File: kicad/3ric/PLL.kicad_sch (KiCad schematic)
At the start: 12 parts

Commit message: update schematics
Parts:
- removed U? (x3): 74LS11, symbol 74xx:74LS11
- removed U_NOT_DECODE? (x2): 74LS14, Package_DIP:DIP-14_W7.62mm_Socket, symbol 74xx:74LS14
- added U? (x3): 74LS20, symbol 74xx:74LS20
- R?: value R430 -> 51
- R?: value R10K -> 30
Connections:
- net GND: now also U?.5 (Inh), U?.10, U?.12, U?.13, U?.7 (GND), U?.9
- net PHI7: now also U?.2 (CP), U?.4 (FOUT)
- net VCC: now also U?.14 (VCC); no longer U?.5 (Inh)
- net at U?.1 (~{MR}): now also U?.6
- net at U?.12 (Q2): now also U?.4, U?.5; no longer U?.3 (RefIn)
- net at U?.13 (Q1): now also U?.2
- net at U?.14 (Q0): now also U?.1
- net at R?.1, U?.13 (PC2): now also U?.9 (VCOin)
- net at C?.1, R?.2: no longer U?.9 (VCOin)
- no-connect marks 0 -> 11
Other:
- moved on the sheet: C?, R?

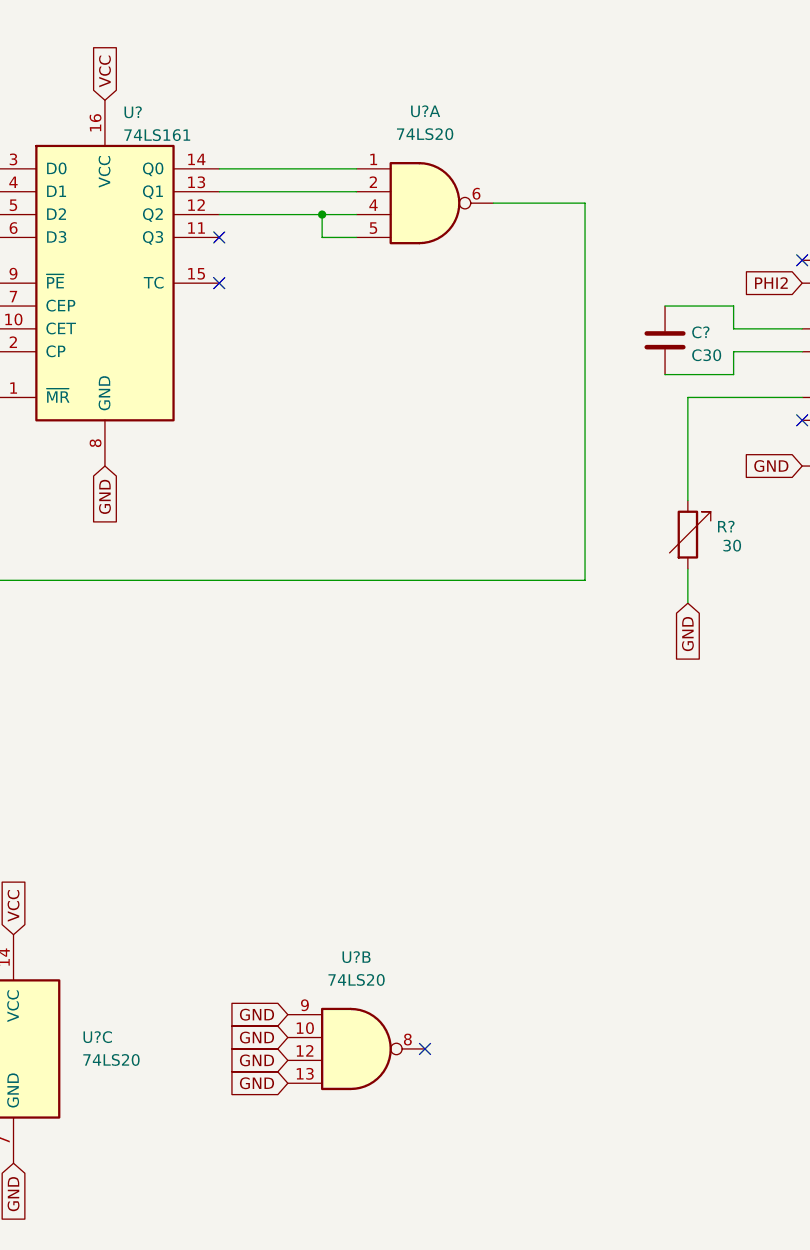
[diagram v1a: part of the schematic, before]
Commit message: upgraded to kicad 8, updates to schematic - added snes controllers, mouse port, many fixes
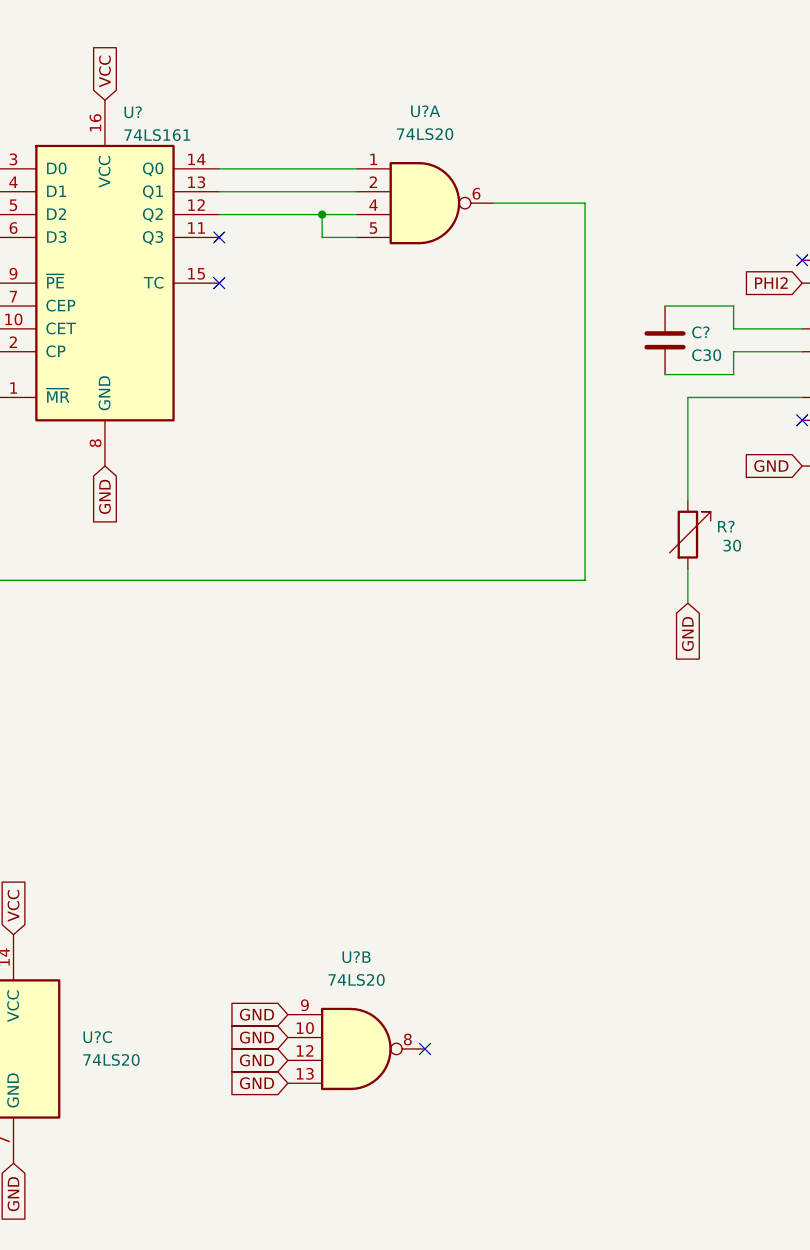
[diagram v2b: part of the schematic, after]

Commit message: wiring continued
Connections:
- net at U?.13 (Q1), U?.2: now also U?.3 (RefIn)
- no-connect marks 11 -> 10
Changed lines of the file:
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@@
 	(paper "A4")
+	(junction
+		(at 101.6 74.93)
+		(diameter 0)
+		(color 0 0 0 0)
+	)
 	(junction
 		(at 198.12 82.55)
@@
 	)
 	(no_connect
-		(at 154.94 82.55)
-	)
-	(no_connect
 		(at 64.77 72.39)
 	)
@@
 	(wire
 		(pts
+			(xy 101.6 62.23) (xy 101.6 74.93)
+		)
+		(stroke
+			(width 0)
+			(type default)
+		)
+	)
+	(wire
+		(pts
 			(xy 180.34 100.33) (xy 184.15 100.33)
 		)
@@
 	(wire
 		(pts
+			(xy 101.6 74.93) (xy 105.41 74.93)
+		)
+		(stroke
+			(width 0)
+			(type default)
+		)
+	)
+	(wire
+		(pts
 			(xy 147.32 92.71) (xy 147.32 95.25)
 		)
@@
 	(wire
 		(pts
+			(xy 154.94 62.23) (xy 101.6 62.23)
+		)
+		(stroke
+			(width 0)
+			(type default)
+		)
+	)
+	(wire
+		(pts
 			(xy 199.39 106.68) (xy 199.39 110.49)
 		)
@@
 	(wire
 		(pts
-			(xy 90.17 74.93) (xy 105.41 74.93)
-		)
-		(stroke
+			(xy 90.17 74.93) (xy 101.6 74.93)
+		)
+		(stroke
+			(width 0)
+			(type default)
+		)
+	)
+	(wire
+		(pts
+			(xy 154.94 82.55) (xy 154.94 62.23)
+		)
+		(stroke

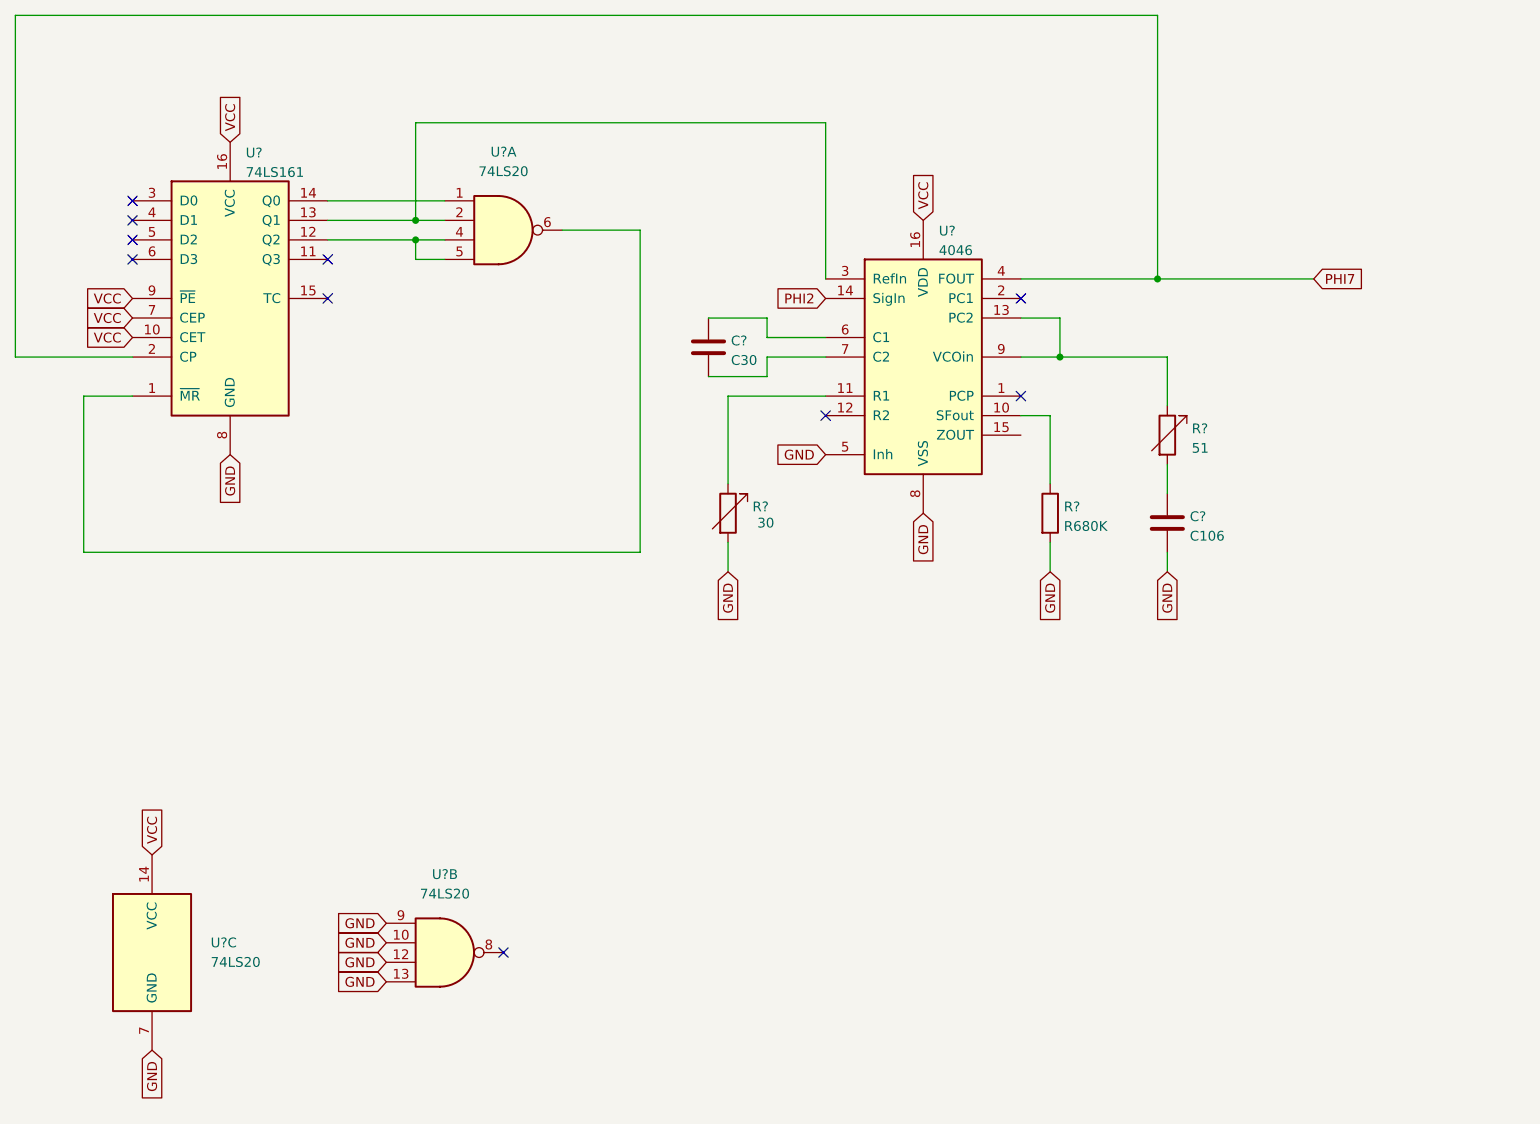
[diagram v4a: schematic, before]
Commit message: update schematic based on breadboard
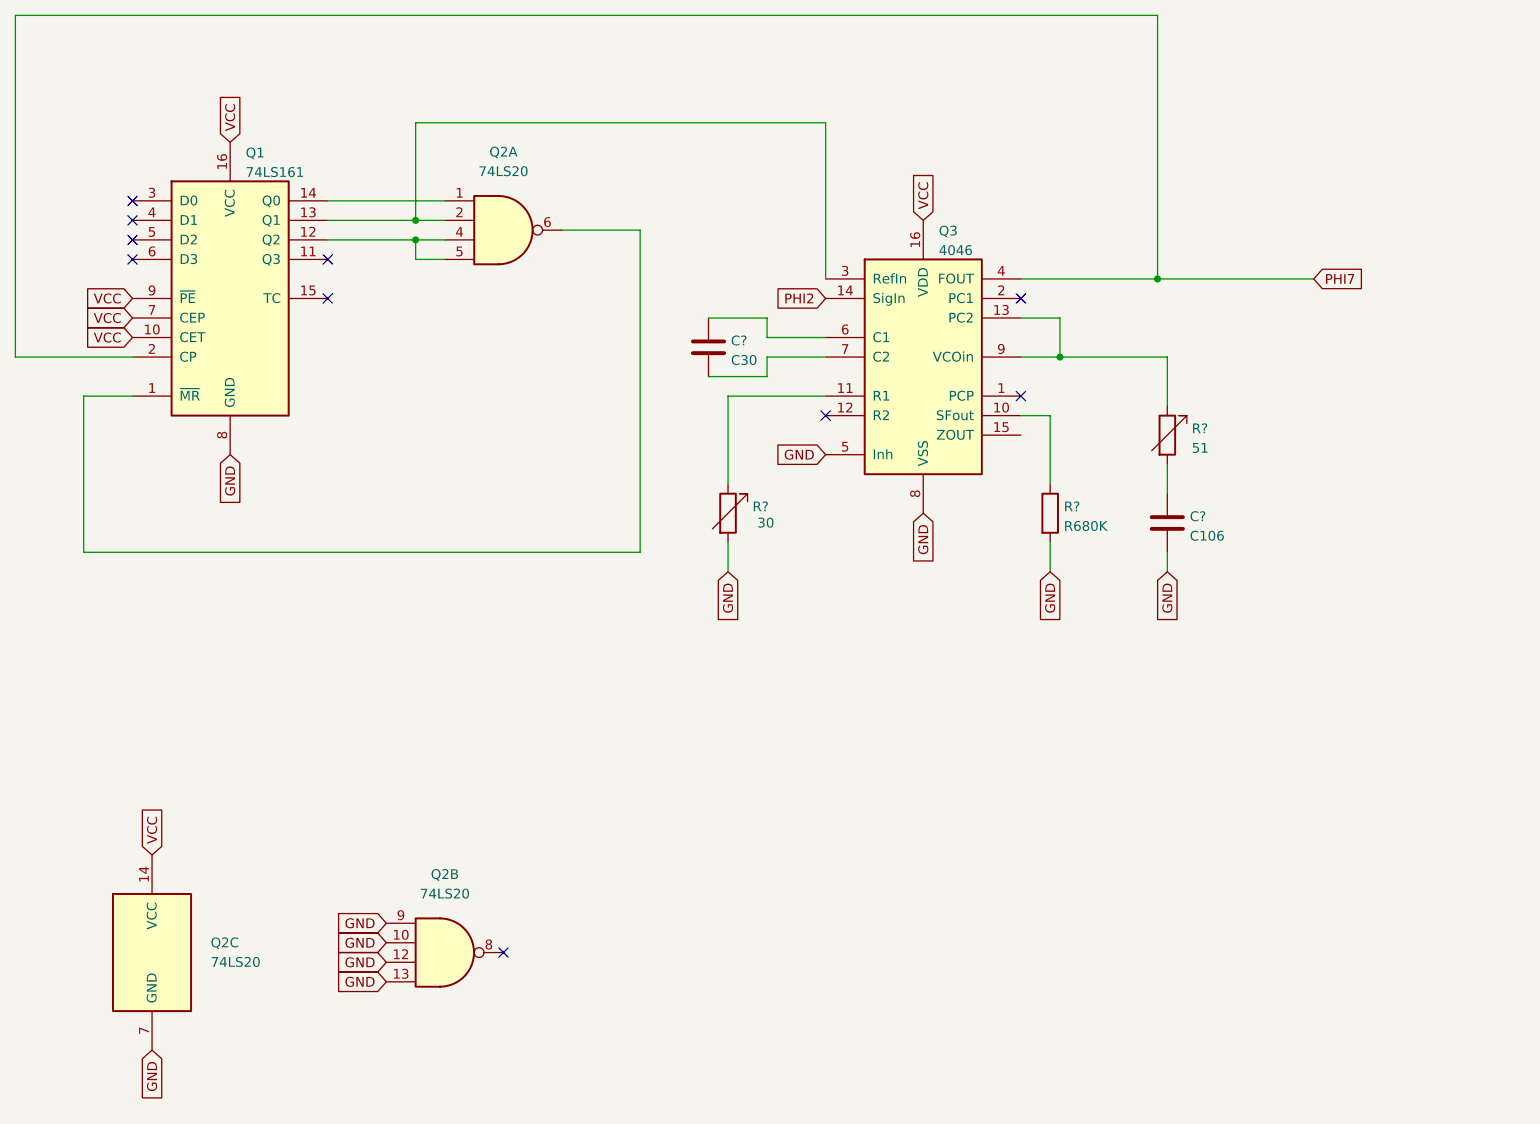
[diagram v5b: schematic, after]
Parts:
- gave numbers to parts that had none: 3
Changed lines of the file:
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@@
 		(dnp no)
 		(fields_autoplaced yes)
-		(property "Reference" "U?"
+		(property "Reference" "Q1"
 			(at 79.4894 66.1502 0)
 			(effects
@@
 			(project "3ric"
 				(path "/e63e39d7-6ac0-4ffd-8aa3-1841a4541b55/f1111e82-0abc-4d93-b82c-5bd5a885becb"
-					(reference "U?")
+					(reference "Q1")
 					(unit 1)
 				)
@@
 		(dnp no)
 		(fields_autoplaced yes)
-		(property "Reference" "U?"
+		(property "Reference" "Q2"
 			(at 113.03 66.04 0)
 			(effects
@@
 			(project "3ric"
 				(path "/e63e39d7-6ac0-4ffd-8aa3-1841a4541b55/f1111e82-0abc-4d93-b82c-5bd5a885becb"
-					(reference "U?")
+					(reference "Q2")
 					(unit 1)
 				)
@@
 		(dnp no)
 		(fields_autoplaced yes)
-		(property "Reference" "U?"
+		(property "Reference" "Q3"
 			(at 169.6594 76.3102 0)
 			(effects
@@
 			(project "3ric"
 				(path "/e63e39d7-6ac0-4ffd-8aa3-1841a4541b55/f1111e82-0abc-4d93-b82c-5bd5a885becb"
-					(reference "U?")
+					(reference "Q3")
 					(unit 1)
 				)
@@
 		(dnp no)
 		(fields_autoplaced yes)
-		(property "Reference" "U?"
+		(property "Reference" "Q2"
 			(at 105.41 160.02 0)
 			(effects
@@
 			(project "3ric"
 				(path "/e63e39d7-6ac0-4ffd-8aa3-1841a4541b55/f1111e82-0abc-4d93-b82c-5bd5a885becb"
-					(reference "U?")
+					(reference "Q2")
 					(unit 2)
 				)
@@
 		(dnp no)
 		(fields_autoplaced yes)
-		(property "Reference" "U?"
+		(property "Reference" "Q2"
 			(at 74.93 168.9099 0)
 			(effects
@@
 			(project "3ric"
 				(path "/e63e39d7-6ac0-4ffd-8aa3-1841a4541b55/f1111e82-0abc-4d93-b82c-5bd5a885becb"
-					(reference "U?")
+					(reference "Q2")
 					(unit 3)
 				)

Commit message: cleaning up of the schematic
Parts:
- C3, C4: renamed from C?; footprint (none) -> Capacitor_THT:C_Axial_L3.8mm_D2.6mm_P7.50mm_Horizontal
- Q1, Q3: footprint (none) -> Package_DIP:DIP-16_W7.62mm_Socket
- Q2: footprint (none) -> Package_DIP:DIP-14_W7.62mm_Socket
- R34, R35, R36: renamed from R?; footprint (none) -> Resistor_THT:R_Axial_DIN0207_L6.3mm_D2.5mm_P7.62mm_Horizontal
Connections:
- no-connect marks 10 -> 11
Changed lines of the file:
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@@
+	)
+	(no_connect
+		(at 180.34 102.87)
 	)
 	(no_connect
@@
 			)
 		)
-		(property "Footprint" ""
+		(property "Footprint" "Package_DIP:DIP-16_W7.62mm_Socket"
 			(at 77.47 85.09 0)
 			(effects
@@
 			)
 		)
-		(property "Footprint" ""
+		(property "Footprint" "Package_DIP:DIP-14_W7.62mm_Socket"
 			(at 113.03 76.2 0)
 			(effects
@@
 		(on_board yes)
 		(dnp no)
-		(property "Reference" "R?"
+		(property "Reference" "R35"
 			(at 185.928 112.1953 0)
 			(effects
@@
 			)
 		)
-		(property "Footprint" ""
+		(property "Footprint" "Resistor_THT:R_Axial_DIN0207_L6.3mm_D2.5mm_P7.62mm_Horizontal"
 			(at 182.372 113.03 90)
 			(effects
@@
 			(project "3ric"
 				(path "/e63e39d7-6ac0-4ffd-8aa3-1841a4541b55/f1111e82-0abc-4d93-b82c-5bd5a885becb"
-					(reference "R?")
+					(reference "R35")
 					(unit 1)
 				)
@@
 		(on_board yes)
 		(dnp no)
-		(property "Reference" "R?"
+		(property "Reference" "R36"
 			(at 202.565 102.0353 0)
 			(effects
@@
 			)
 		)
-		(property "Footprint" ""
+		(property "Footprint" "Resistor_THT:R_Axial_DIN0207_L6.3mm_D2.5mm_P7.62mm_Horizontal"
 			(at 197.612 102.87 90)
 			(effects
@@
 			(project "3ric"
 				(path "/e63e39d7-6ac0-4ffd-8aa3-1841a4541b55/f1111e82-0abc-4d93-b82c-5bd5a885becb"
-					(reference "R?")
+					(reference "R36")
 					(unit 1)
 				)
@@
 		(dnp no)
 		(fields_autoplaced yes)
-		(property "Reference" "C?"
+		(property "Reference" "C4"
 			(at 202.311 113.4653 0)
 			(effects
@@
 			)
 		)
-		(property "Footprint" ""
+		(property "Footprint" "Capacitor_THT:C_Axial_L3.8mm_D2.6mm_P7.50mm_Horizontal"
 			(at 200.3552 118.11 0)
 			(effects
@@
 			(project "3ric"
 				(path "/e63e39d7-6ac0-4ffd-8aa3-1841a4541b55/f1111e82-0abc-4d93-b82c-5bd5a885becb"
-					(reference "C?")
+					(reference "C4")
 					(unit 1)
 				)
@@
 		(on_board yes)
 		(dnp no)
-		(property "Reference" "R?"
+		(property "Reference" "R34"
 			(at 145.415 112.1953 0)
 			(effects
@@
 			)
 		)
-		(property "Footprint" ""
+		(property "Footprint" "Resistor_THT:R_Axial_DIN0207_L6.3mm_D2.5mm_P7.62mm_Horizontal"
 			(at 140.462 113.03 90)
 			(effects
@@
 			(project "3ric"
 				(path "/e63e39d7-6ac0-4ffd-8aa3-1841a4541b55/f1111e82-0abc-4d93-b82c-5bd5a885becb"
-					(reference "R?")
+					(reference "R34")
 					(unit 1)
 				)
@@
 			)
 		)
-		(property "Footprint" ""
+		(property "Footprint" "Package_DIP:DIP-16_W7.62mm_Socket"
 			(at 167.64 92.71 0)
 			(effects
@@
 			)
 		)
-		(property "Footprint" ""
+		(property "Footprint" "Package_DIP:DIP-14_W7.62mm_Socket"
 			(at 105.41 170.18 0)
 			(effects
@@
 			)
 		)
-		(property "Footprint" ""
+		(property "Footprint" "Package_DIP:DIP-14_W7.62mm_Socket"
 			(at 67.31 170.18 0)
 			(effects
@@
 		(dnp no)
 		(fields_autoplaced yes)
-		(property "Reference" "C?"
+		(property "Reference" "C3"
 			(at 142.621 90.6053 0)
 			(effects
@@
 			)
 		)
-		(property "Footprint" ""
+		(property "Footprint" "Capacitor_THT:C_Axial_L3.8mm_D2.6mm_P7.50mm_Horizontal"
 			(at 140.6652 95.25 0)
 			(effects
@@
 			(project "3ric"
 				(path "/e63e39d7-6ac0-4ffd-8aa3-1841a4541b55/f1111e82-0abc-4d93-b82c-5bd5a885becb"
-					(reference "C?")
+					(reference "C3")
 					(unit 1)
 				)

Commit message: updated schematics and PCB PNG of the breadboard layout
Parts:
- C3: footprint Capacitor_THT:C_Axial_L3.8mm_D2.6mm_P7.50mm_Horizontal -> Capacitor_SMD:C_0805_2012Metric_Pad1.18x1.45mm_HandSolder
- C4: footprint Capacitor_THT:C_Axial_L3.8mm_D2.6mm_P7.50mm_Horizontal -> Capacitor_SMD:C_0603_1608Metric_Pad1.08x0.95mm_HandSolder
- R34, R36: footprint Resistor_THT:R_Axial_DIN0207_L6.3mm_D2.5mm_P7.62mm_Horizontal -> Resistor_SMD:R_0402_1005Metric_Pad0.72x0.64mm_HandSolder
- R35: footprint Resistor_THT:R_Axial_DIN0207_L6.3mm_D2.5mm_P7.62mm_Horizontal -> Resistor_SMD:R_0603_1608Metric_Pad0.98x0.95mm_HandSolder
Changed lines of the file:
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@@
 			)
 		)
-		(property "Footprint" "Resistor_THT:R_Axial_DIN0207_L6.3mm_D2.5mm_P7.62mm_Horizontal"
+		(property "Footprint" "Resistor_SMD:R_0603_1608Metric_Pad0.98x0.95mm_HandSolder"
 			(at 182.372 113.03 90)
 			(effects
@@
 			)
 		)
-		(property "Footprint" "Resistor_THT:R_Axial_DIN0207_L6.3mm_D2.5mm_P7.62mm_Horizontal"
+		(property "Footprint" "Resistor_SMD:R_0402_1005Metric_Pad0.72x0.64mm_HandSolder"
 			(at 197.612 102.87 90)
 			(effects
@@
 			)
 		)
-		(property "Footprint" "Capacitor_THT:C_Axial_L3.8mm_D2.6mm_P7.50mm_Horizontal"
+		(property "Footprint" "Capacitor_SMD:C_0603_1608Metric_Pad1.08x0.95mm_HandSolder"
 			(at 200.3552 118.11 0)
 			(effects
@@
 			)
 		)
-		(property "Footprint" "Resistor_THT:R_Axial_DIN0207_L6.3mm_D2.5mm_P7.62mm_Horizontal"
+		(property "Footprint" "Resistor_SMD:R_0402_1005Metric_Pad0.72x0.64mm_HandSolder"
 			(at 140.462 113.03 90)
 			(effects
@@
 			)
 		)
-		(property "Footprint" "Capacitor_THT:C_Axial_L3.8mm_D2.6mm_P7.50mm_Horizontal"
+		(property "Footprint" "Capacitor_SMD:C_0805_2012Metric_Pad1.18x1.45mm_HandSolder"
 			(at 140.6652 95.25 0)
 			(effects

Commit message: v2 pcb
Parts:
- removed R34: 30, Resistor_SMD:R_0402_1005Metric_Pad0.72x0.64mm_HandSolder, symbol Device:R_Variable
- removed R35: R680K, Resistor_SMD:R_0603_1608Metric_Pad0.98x0.95mm_HandSolder, symbol Device:R
- removed R36: 51, Resistor_SMD:R_0402_1005Metric_Pad0.72x0.64mm_HandSolder, symbol Device:R_Variable
- added R12001, R12002, R12003: R_Variable, Potentiometer_THT:Potentiometer_Piher_PT-6-V_Vertical, symbol Device:R_Variable
- C3: value C30 -> C60
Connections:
- net GND: now also R12002.2, R12003.2
- net at Q3.10 (SFout): now also R12003.1
- net at Q3.13 (PC2): now also R12001.1; no longer Q3.9 (VCOin)
- net at C4.1: now also Q3.9 (VCOin), R12001.2
- net at Q3.11 (R1): now also R12002.1
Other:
- moved on the sheet: C4
